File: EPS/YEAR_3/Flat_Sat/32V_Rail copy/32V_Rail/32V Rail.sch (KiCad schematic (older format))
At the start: 35 parts, among them J1 Vin, J2 SCL, J3 Supply Voltage, J4 SDA, J6 Conn_01x03_Male, U1 INA226, U1 LT3571, U2 TPS26600, U3 LM335, U4 STM32L1

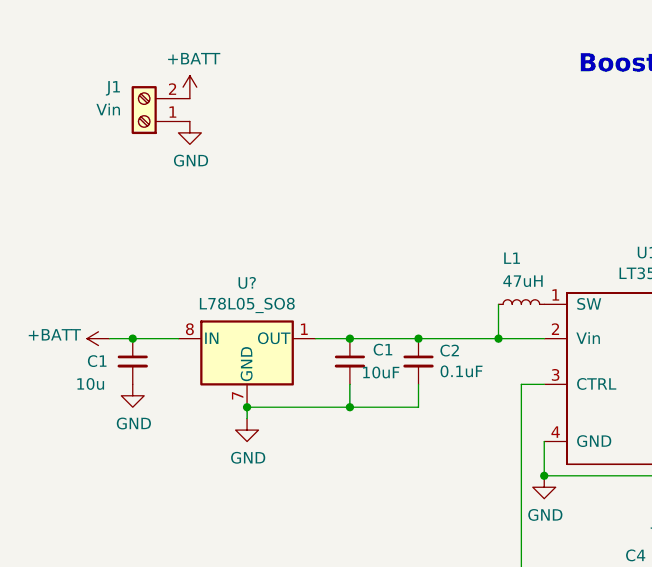
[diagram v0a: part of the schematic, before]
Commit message: 35V rail updates
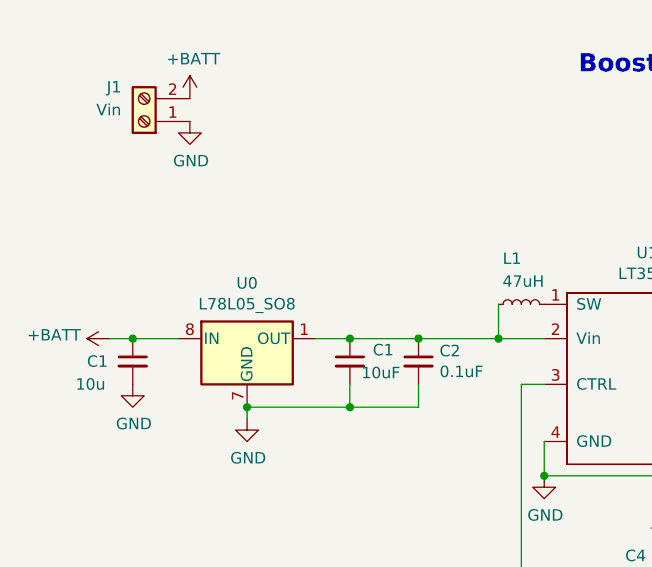
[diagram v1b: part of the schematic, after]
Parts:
- gave numbers to parts that had none: 1
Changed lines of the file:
@@
 Power Switch (1A Limit)
 $Comp
-L Regulator_Linear:L78L05_SO8 U?
+L Regulator_Linear:L78L05_SO8 U0
 U 1 1 5EBE4497
 P 1600 2800
-F 0 "U?" H 1600 3042 50  0000 C CNN
+F 0 "U0" H 1600 3042 50  0000 C CNN
 F 1 "L78L05_SO8" H 1600 2951 50  0000 C CNN
 F 2 "Package_SO:SOIC-8_3.9x4.9mm_P1.27mm" H 1700 3000 50  0001 C CIN

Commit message: changed file name
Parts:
- removed C1: 10uF, symbol Device:C_Small
- removed C2: 0.1uF, symbol Device:C_Small
- removed U0: L78L05_SO8, Package_SO:SOIC-8_3.9x4.9mm_P1.27mm, symbol Regulator_Linear:L78L05_SO8
- removed U1: LT3571, symbol 32V-Rail-rescue:LT3571
- removed U2: TPS26600, Package_SO:TSSOP-16_4.4x5mm_P0.65mm, symbol 32V-Rail-rescue:TPS26600-SlugSat_Power_Symbol_Library-32V-Rail-rescue
- removed U3: LM335, symbol 32V-Rail-rescue:LM335
- added U1: LT3571, symbol power:LT3571
- added U2: TPS26600, symbol power:TPS26600
- added U3: LM335, symbol power:LM335
- U4: symbol 32V-Rail-rescue:STM32L1 -> 32V-Rail-rescue:STM32L1-32V-Rail-rescue
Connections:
- wire segments 96 -> 89
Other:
- note added: "ADC"
- note added: "DAC"
- note added: "Vin = 3.9V"
- moved on the sheet: C1, J6, R2, R3, R_ILIM
